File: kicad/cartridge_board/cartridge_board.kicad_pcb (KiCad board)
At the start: 4 copper layers, 12.9 x 11.6 mm, 3 parts, among them J1 Conn_02x04_Odd_Even, U1 ATtiny10

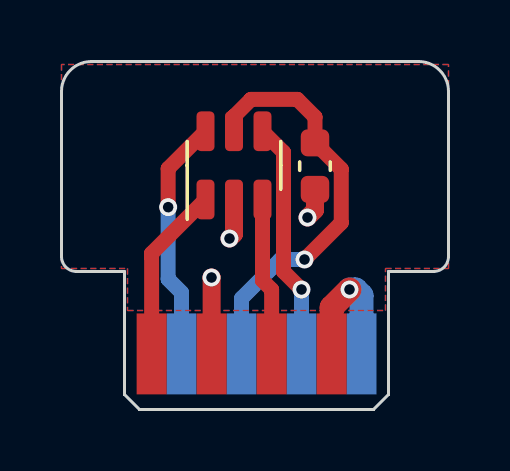
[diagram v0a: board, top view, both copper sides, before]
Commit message: pcbs: improve powering scheme, redesign cartridge; 3dcad: update whole housing
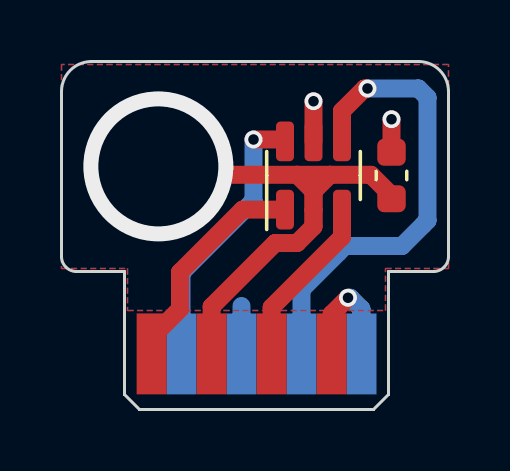
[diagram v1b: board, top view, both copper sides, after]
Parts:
- moved U1 2.67 mm to (131.1, 83.8)
- moved C1 2.57 mm to (133.7, 83.8)
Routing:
- net GND: track 4.95 -> 17.1 mm, vias 3 -> 1
- net VCC: track 13.8 -> 4.03 mm, vias 1 -> 2
- net Net-(J1-Pin_6): track 7.96 -> 15.7 mm
- net Net-(J1-Pin_1): track 5.89 -> 7.48 mm
- net Net-(J1-Pin_2): track 8.12 -> 9.22 mm
- net Net-(J1-Pin_7): track 4.82 -> 4.20 mm
- net Net-(J1-Pin_5): track 5.27 -> 5.78 mm
- added copper zone on F.Cu, net GND
- added copper zone on B.Cu, net VCC
- removed copper zone on B.Cu, net GND
- removed copper zone on F.Cu, net VCC

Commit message: flip cartridge pcb
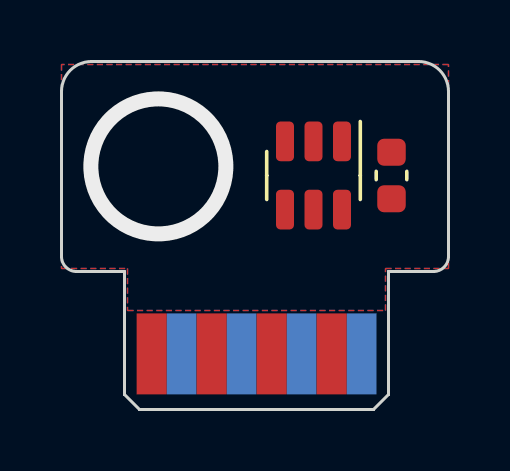
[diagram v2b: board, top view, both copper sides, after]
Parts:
- turned U1 to -90 degrees
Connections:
- J1 pad 2: Net-(J1-Pin_2) -> Net-(J1-Pin_1)
- J1 pad 3: GND -> ATTINY_PB1
- J1 pad 4: VCC -> ATTINY_PB2
- J1 pad 5: Net-(J1-Pin_5) -> GND
- J1 pad 6: Net-(J1-Pin_6) -> VCC
- J1 pad 7: Net-(J1-Pin_7) -> ATTINY_PB0
- J1 pad 8: Net-(J1-Pin_7) -> ATTINY_PB3
- U1 pad 1: Net-(J1-Pin_1) -> ATTINY_PB0
- U1 pad 3: Net-(J1-Pin_5) -> ATTINY_PB1
- U1 pad 4: Net-(J1-Pin_6) -> ATTINY_PB2
- U1 pad 6: Net-(J1-Pin_2) -> ATTINY_PB3
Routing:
- net GND: track 17.1 -> 0.00 mm
- net Net-(J1-Pin_6): track 15.7 -> 0.00 mm, vias 1 -> 0
- net Net-(J1-Pin_2): track 9.22 -> 0.00 mm, vias 1 -> 0
- net Net-(J1-Pin_1): track 7.48 -> 0.00 mm
- net Net-(J1-Pin_5): track 5.78 -> 0.00 mm
- net Net-(J1-Pin_7): track 4.20 -> 0.00 mm, vias 1 -> 0
- net VCC: track 4.03 -> 0.00 mm, vias 2 -> 0

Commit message: cartridge pcb panelized; smol fixes to baseboard pcb
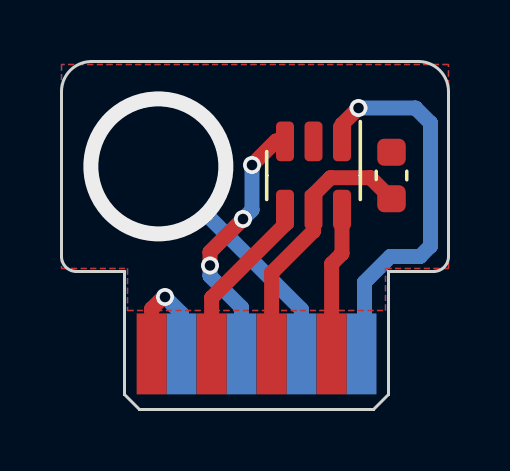
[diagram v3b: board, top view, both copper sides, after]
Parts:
- turned C1 to 90 degrees
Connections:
- J1 pad 3: ATTINY_PB1 -> ATTINY_PB2
- J1 pad 4: ATTINY_PB2 -> ATTINY_PB1
- J1 pad 5: GND -> VCC
- J1 pad 6: VCC -> GND
- J1 pad 7: ATTINY_PB0 -> ATTINY_PB3
- J1 pad 8: ATTINY_PB3 -> ATTINY_PB0
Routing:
- net ATTINY_PB0: track 0.00 -> 13.2 mm, vias 0 -> 1
- net VCC: track 0.00 -> 9.01 mm
- net ATTINY_PB1: track 0.00 -> 8.75 mm, vias 0 -> 3
- net GND: track 0.00 -> 8.23 mm
- net ATTINY_PB2: track 0.00 -> 5.82 mm
- net ATTINY_PB3: track 0.00 -> 4.95 mm
- net Net-(J1-Pin_1): track 0.00 -> 4.23 mm, vias 0 -> 1
